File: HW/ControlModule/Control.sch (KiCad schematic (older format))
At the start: 88 parts, among them J1 Conn_01x03, J2 Conn_01x03, J3 Conn_01x03, J4 Conn_01x03, J5 Conn_01x03, J6 Conn_01x03, J7 Conn_01x03, J8 Conn_01x03, U1 AD8629, U2 STM32L496VGTx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

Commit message: updates
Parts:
- C24, C25: value 20pF -> 1pF
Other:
- note added: "NOTE:\nIncreasing C24/C25 will increase \npower cycle delay time"
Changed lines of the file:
@@
 P 20150 9250
 F 0 "C24" H 20036 9204 50  0000 R CNN
-F 1 "20pF" H 20036 9295 50  0000 R CNN
+F 1 "1pF" H 20036 9295 50  0000 R CNN
 F 2 "Capacitor_SMD:C_0805_2012Metric_Pad1.15x1.40mm_HandSolder" H 20188 9100 50  0001 C CNN
 F 3 "~" H 20150 9250 50  0001 C CNN
@@
 P 20500 9250
 F 0 "C25" H 20615 9296 50  0000 L CNN
-F 1 "20pF" H 20615 9205 50  0000 L CNN
+F 1 "1pF" H 20615 9205 50  0000 L CNN
 F 2 "Capacitor_SMD:C_0805_2012Metric_Pad1.15x1.40mm_HandSolder" H 20538 9100 50  0001 C CNN
 F 3 "~" H 20500 9250 50  0001 C CNN
@@
 $EndComp
 NoConn ~ 11900 5800
+Text Notes 18675 9650 0    50   ~ 0
+NOTE:\nIncreasing C24/C25 will increase \npower cycle delay time
 $EndSCHEMATC

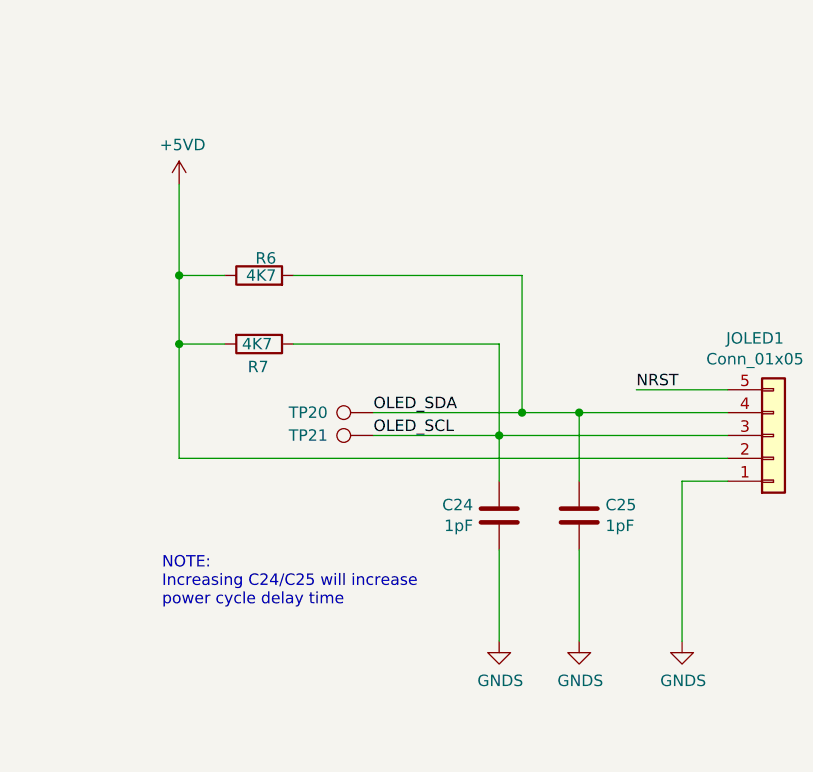
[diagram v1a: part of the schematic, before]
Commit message: updated power supply and front panel
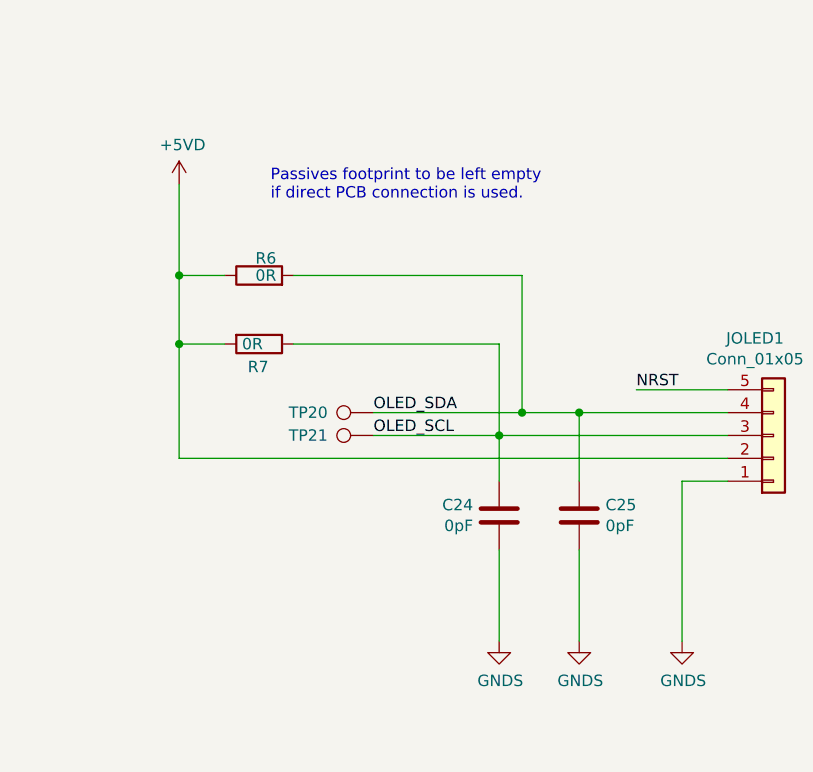
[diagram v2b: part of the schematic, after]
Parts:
- C24, C25: value 1pF -> 0pF
- R6, R7: value 4K7 -> 0R
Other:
- note added: "Passives footprint to be left empty\nif direct PCB connection is used."
- note removed: "NOTE:\nIncreasing C24/C25 will increase \npower cycle delay time"
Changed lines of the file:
@@
 P 19100 8200
 F 0 "R6" V 19175 8125 50  0000 L CNN
-F 1 "4K7" V 19100 8125 50  0000 L CNN
+F 1 "0R" V 19100 8125 50  0000 L CNN
 F 2 "Resistor_SMD:R_0805_2012Metric_Pad1.15x1.40mm_HandSolder" V 19030 8200 50  0001 C CNN
 F 3 "~" H 19100 8200 50  0001 C CNN
@@
 P 19100 8500
 F 0 "R7" V 19200 8450 50  0000 L CNN
-F 1 "4K7" V 19100 8425 50  0000 L CNN
+F 1 "0R" V 19100 8425 50  0000 L CNN
 F 2 "Resistor_SMD:R_0805_2012Metric_Pad1.15x1.40mm_HandSolder" V 19030 8500 50  0001 C CNN
 F 3 "~" H 19100 8500 50  0001 C CNN
@@
 P 20150 9250
 F 0 "C24" H 20036 9204 50  0000 R CNN
-F 1 "1pF" H 20036 9295 50  0000 R CNN
+F 1 "0pF" H 20036 9295 50  0000 R CNN
 F 2 "Capacitor_SMD:C_0805_2012Metric_Pad1.15x1.40mm_HandSolder" H 20188 9100 50  0001 C CNN
 F 3 "~" H 20150 9250 50  0001 C CNN
@@
 P 20500 9250
 F 0 "C25" H 20615 9296 50  0000 L CNN
-F 1 "1pF" H 20615 9205 50  0000 L CNN
+F 1 "0pF" H 20615 9205 50  0000 L CNN
 F 2 "Capacitor_SMD:C_0805_2012Metric_Pad1.15x1.40mm_HandSolder" H 20538 9100 50  0001 C CNN
 F 3 "~" H 20500 9250 50  0001 C CNN
@@
 $EndComp
 NoConn ~ 11900 5800
-Text Notes 18675 9650 0    50   ~ 0
-NOTE:\nIncreasing C24/C25 will increase \npower cycle delay time
+Text Notes 19150 7875 0    50   ~ 0
+Passives footprint to be left empty\nif direct PCB connection is used.
 $EndSCHEMATC
